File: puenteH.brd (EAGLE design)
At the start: 100 x 80 mm, 20 parts, among them IC1 LM393N, Q1 IRF4905, Q2 IRLZ44Z, Q3 IRLZ44Z, Q4 IRF4905, Q5 IRF540, Q6 IRF540, Q7 IRF9530, Q8 IRF9530

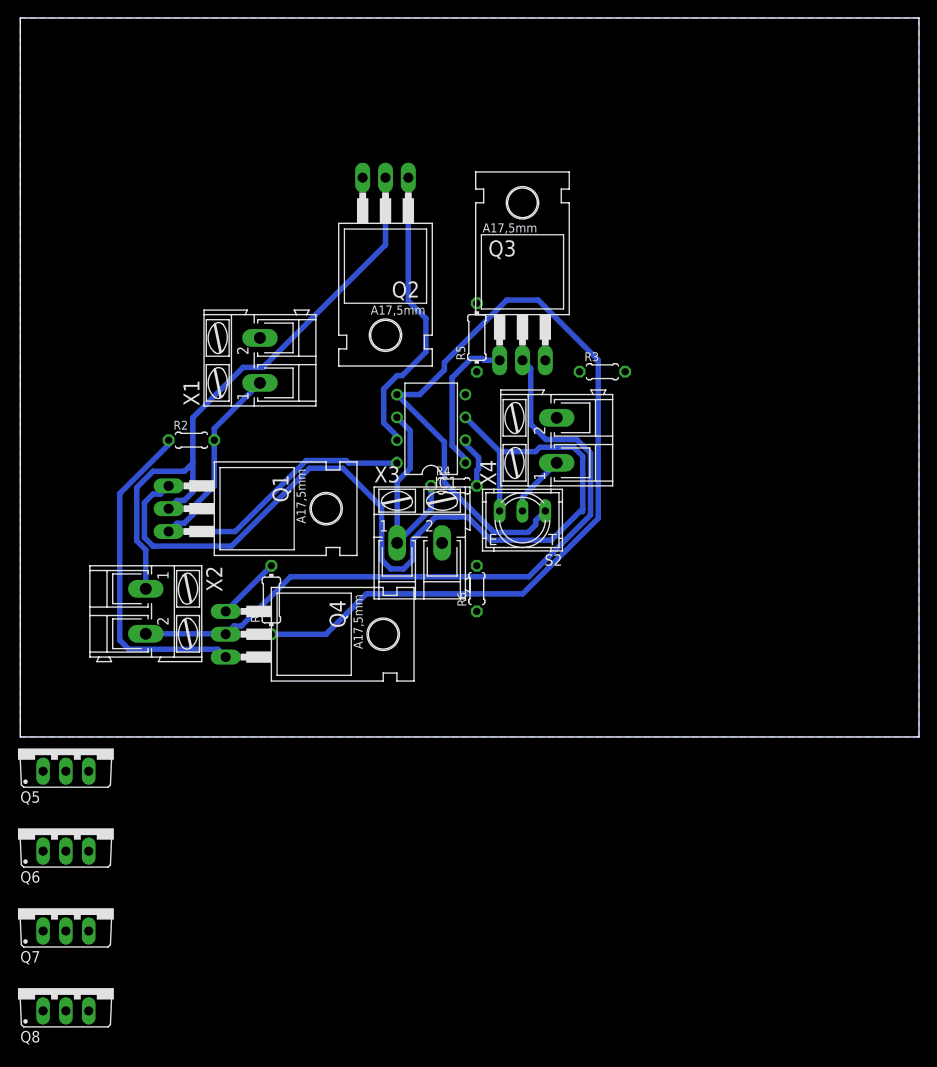
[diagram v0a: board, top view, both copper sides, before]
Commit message: Board using real components ready, just need to verify that they in fact exist (or that it is possible to find them at the store)
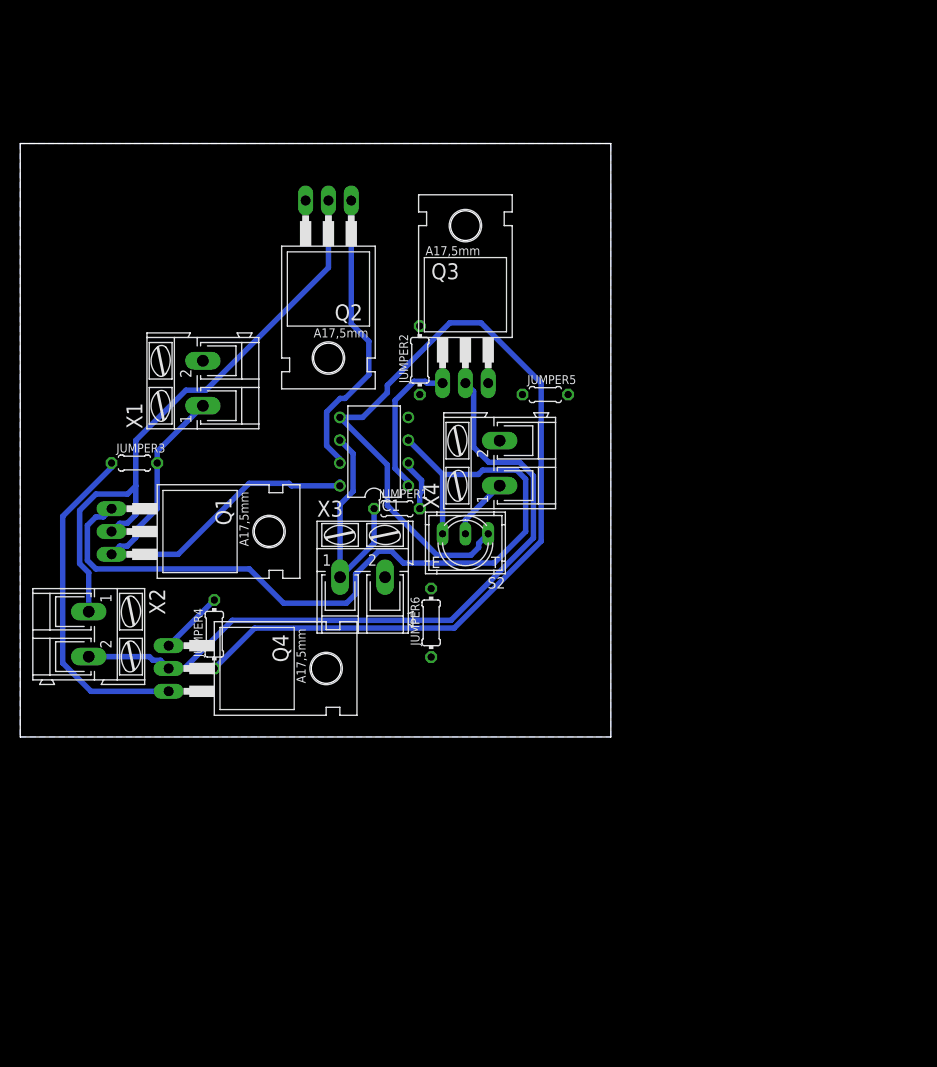
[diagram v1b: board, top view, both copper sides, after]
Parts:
- removed Q5, Q6: IRF540, transistor-power:TO220BV
- removed Q7, Q8: IRF9530, transistor-power:TO220BV
- removed R1, R5: (no value), rcl:0204/7
- removed R2, R3, R4, R6: (no value), rcl:0204/5
- added JUMPER1, JUMPER3, JUMPER5: (no value), rcl:0204/5
- added JUMPER2, JUMPER4, JUMPER6: (no value), rcl:0204/7
- moved Q4 7.41 mm to (22.9, 7.62)
- moved X3 7.41 mm to (38.1, 17.8)
- moved IC1 6.84 mm to (39.4, 31.8)
- moved Q2 6.84 mm to (34.3, 53.3)
- moved Q3 6.84 mm to (49.5, 45.7)
- moved S2 6.84 mm to (49.5, 21.6)
- moved X1 6.84 mm to (20.3, 39.4)
- moved X2 6.84 mm to (7.62, 11.4)
- moved Q1 6.84 mm to (16.5, 22.9)
- moved X4 6.84 mm to (53.3, 30.5)
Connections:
- net 0: now also JUMPER2.1, JUMPER2.2, JUMPER5.1, JUMPER5.2, JUMPER6.1, JUMPER6.2; no longer R3.1, R3.2, R5.1, R5.2, R6.1, R6.2
- net IZQ: now also JUMPER4.1, JUMPER4.2; no longer R1.1, R1.2
- net PWM: now also JUMPER1.1, JUMPER1.2; no longer R4.1, R4.2
- net VCC: now also JUMPER3.1, JUMPER3.2; no longer R2.1, R2.2
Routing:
- net DER: track 102.4 -> 91.5 mm
- net PWM: track 28.9 -> 31.4 mm
- net MOTOR_DER: track 77.4 -> 78.4 mm
- net VCC: track 87.5 -> 88.1 mm
- net IZQ: track 123.3 -> 123.8 mm
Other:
- board size 100 x 80 mm -> 65.7 x 66 mm
